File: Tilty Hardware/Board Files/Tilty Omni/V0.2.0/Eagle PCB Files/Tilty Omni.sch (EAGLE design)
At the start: 11 parts, among them U1 TEENSY_3.0_ALLPINS

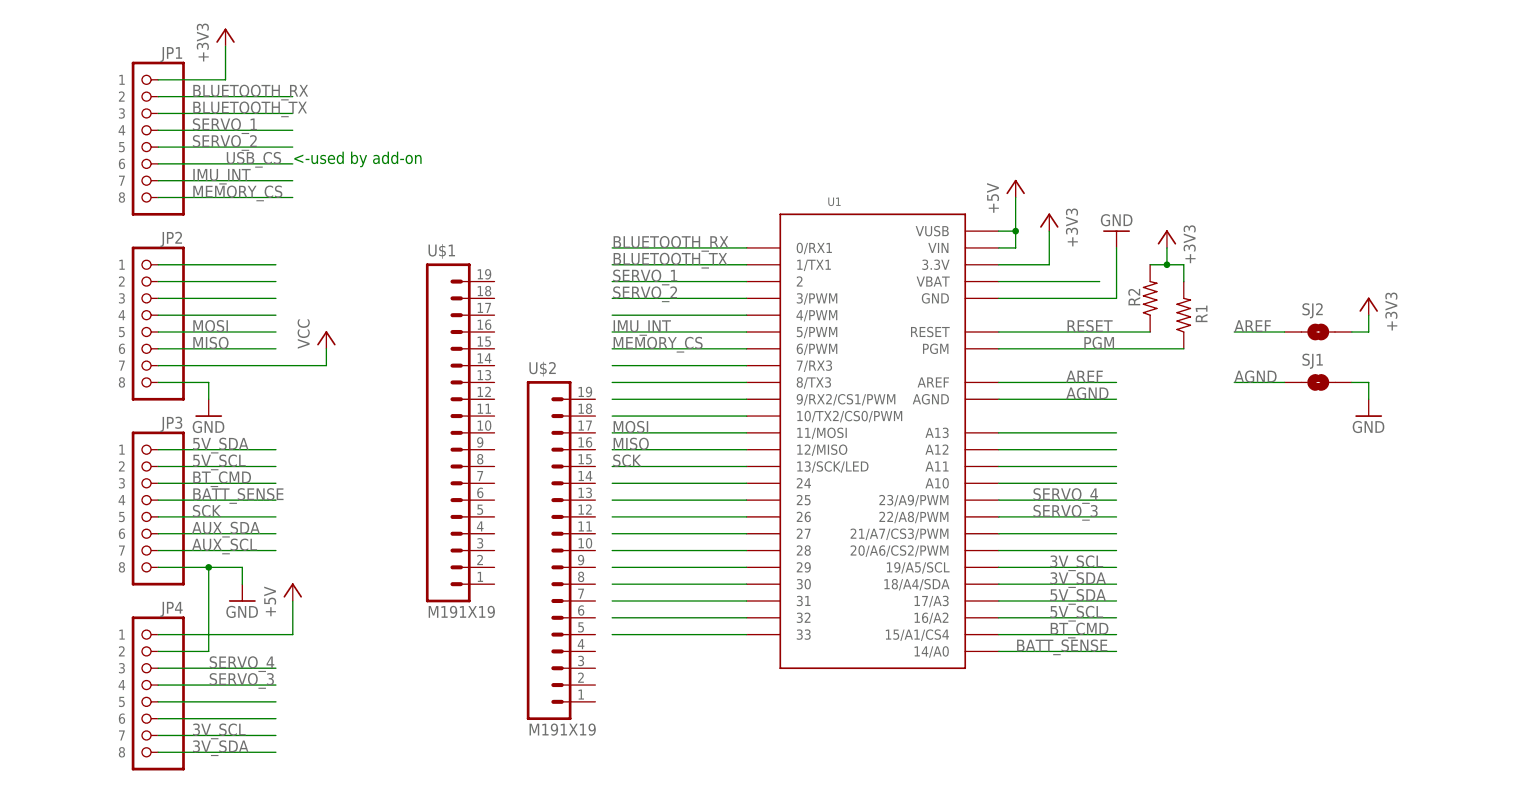
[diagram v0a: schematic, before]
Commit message: Updated Tilty Omni pinout and removed Eagle backup files,as that's what GitHub is for
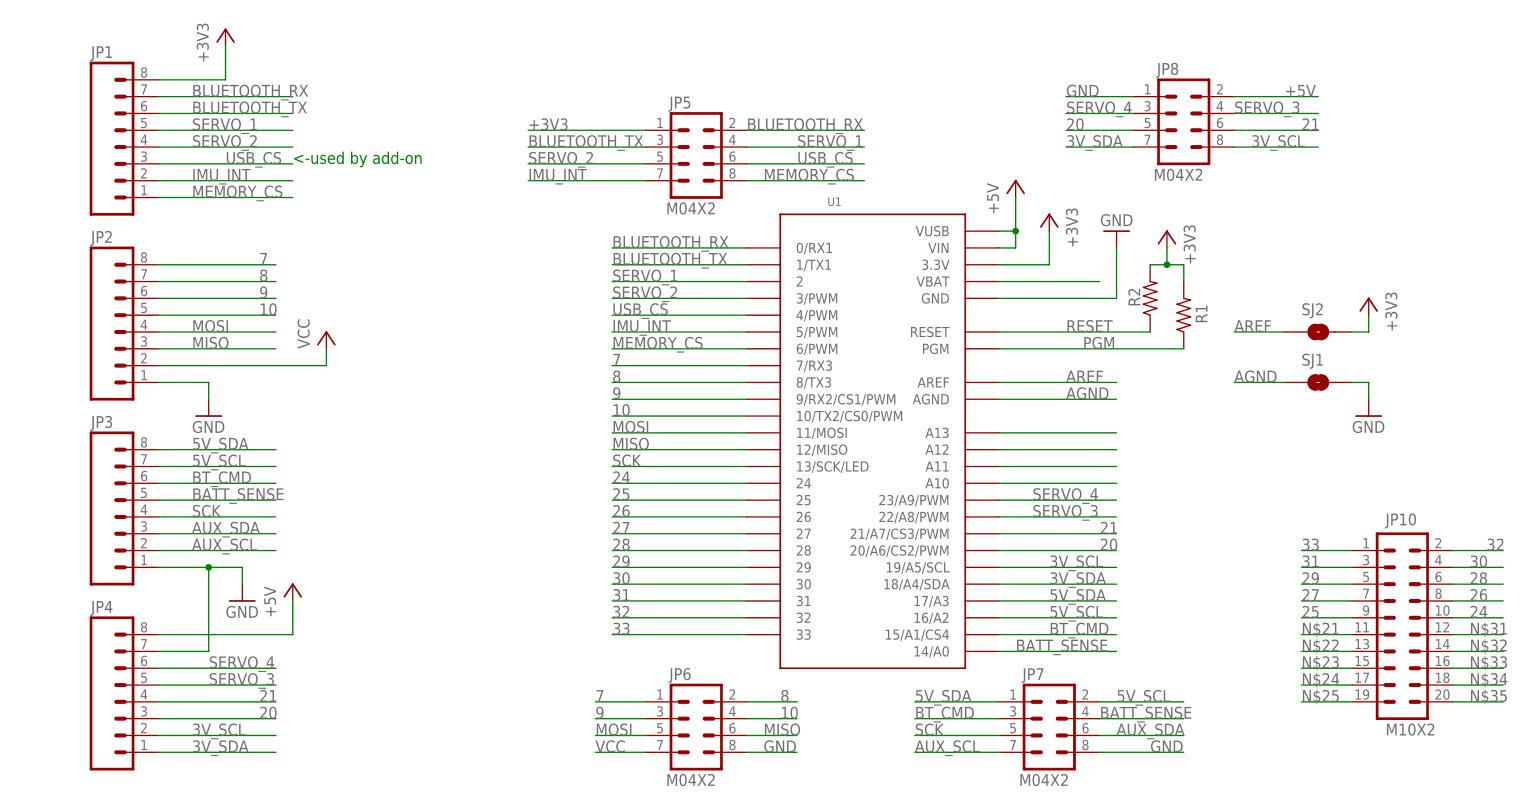
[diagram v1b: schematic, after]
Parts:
- removed U$1, U$2: M191X19, SparkFun-Connectors:M191X19
- added JP10: M10X2, SparkFun-Connectors:M10X2
- added JP5, JP6, JP7, JP8: M04X2, SparkFun-Connectors:M04X2
- JP1, JP2, JP3, JP4: value 8-PIN_HEADER -> (none); device My Parts:8-PIN_HEADER -> SparkFun-Connectors:M081X08
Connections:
- net N$14 renamed A13
- removed net N$1: U1.24
- removed net N$10: U1.33
- removed net N$2: U1.25
- removed net N$3: U1.26
- removed net N$4: U1.27
- removed net N$5: U1.28
- removed net N$6: U1.29
- removed net N$7: U1.30
- removed net N$8: U1.31
- removed net N$9: U1.32
- new net 24: JP10.10, U1.24
- new net 25: JP10.9, U1.25
- new net 26: JP10.8, U1.26
- new net 27: JP10.7, U1.27
- new net 28: JP10.6, U1.28
- new net 29: JP10.5, U1.29
- new net 30: JP10.4, U1.30
- new net 31: JP10.3, U1.31
- new net 32: JP10.2, U1.32
- new net 33: JP10.1, U1.33
- new net N$21: JP10.11
- new net N$22: JP10.13
- new net N$23: JP10.15
- new net N$24: JP10.17
- new net N$25: JP10.19
- new net N$31: JP10.12
- new net N$32: JP10.14
- new net N$33: JP10.16
- new net N$34: JP10.18
- new net N$35: JP10.20
- net +3V3: now also JP1.8, JP5.1; no longer JP1.1
- net +5V: now also JP4.8, JP8.2; no longer JP4.1
- net 10: now also JP2.5, JP6.4; no longer JP2.4
- net 20: now also JP4.3, JP8.5; no longer JP4.6
- net 21: now also JP4.4, JP8.6; no longer JP4.5
- net 3V_SCL: now also JP4.2, JP8.8; no longer JP4.7
- net 3V_SDA: now also JP4.1, JP8.7; no longer JP4.8
- net 5V_SCL: now also JP3.7, JP7.2; no longer JP3.2
- net 5V_SDA: now also JP3.8, JP7.1; no longer JP3.1
- net 7: now also JP2.8, JP6.1; no longer JP2.1
- net 8: now also JP2.7, JP6.2; no longer JP2.2
- net 9: now also JP2.6, JP6.3; no longer JP2.3
- net AUX_SCL: now also JP3.2, JP7.7; no longer JP3.7
- net AUX_SDA: now also JP3.3, JP7.6; no longer JP3.6
- net BATT_SENSE: now also JP3.5, JP7.4; no longer JP3.4
- net BLUETOOTH_RX: now also JP1.7, JP5.2; no longer JP1.2
- net BLUETOOTH_TX: now also JP1.6, JP5.3; no longer JP1.3
- net BT_CMD: now also JP3.6, JP7.3; no longer JP3.3
- net GND: now also JP2.1, JP3.1, JP4.7, JP6.8, JP7.8, JP8.1; no longer JP2.8, JP3.8, JP4.2
- net IMU_INT: now also JP1.2, JP5.7; no longer JP1.7
- net MEMORY_CS: now also JP1.1, JP5.8; no longer JP1.8
- net MISO: now also JP2.3, JP6.6; no longer JP2.6
- net MOSI: now also JP2.4, JP6.5; no longer JP2.5
- net SCK: now also JP3.4, JP7.5; no longer JP3.5
- net SERVO_1: now also JP1.5, JP5.4; no longer JP1.4
- net SERVO_2: now also JP1.4, JP5.5; no longer JP1.5
- net SERVO_3: now also JP4.5, JP8.4; no longer JP4.4
- net SERVO_4: now also JP4.6, JP8.3; no longer JP4.3
- net USB_CS: now also JP1.3, JP5.6; no longer JP1.6
- net VCC: now also JP2.2, JP6.7; no longer JP2.7
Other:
- moved on the sheet: JP1, JP2, JP3, JP4

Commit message: Tilty Omni work
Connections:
- net N$21 renamed A12
- net N$22 renamed A10
- net N$32 renamed A11
- removed net N$23: JP10.15
- removed net N$24: JP10.17
- removed net N$25: JP10.19
- removed net N$31: JP10.12
- removed net N$33: JP10.16
- removed net N$34: JP10.18
- removed net N$35: JP10.20
- net +3V3: now also JP10.19
- net A13: now also JP10.12
- net AGND: now also JP10.16
- net AREF: now also JP10.15
- net GND: now also JP10.20
- net PGM: now also JP10.17
- net RESET: now also JP10.18
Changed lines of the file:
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@@
 <label x="142.24" y="101.6" size="1.778" layer="95"/>
+</segment>
+<segment>
+<pinref part="JP10" gate="G$1" pin="20"/>
+<wire x1="200.66" y1="10.16" x2="208.28" y2="10.16" width="0.1524" layer="91"/>
+<label x="203.2" y="10.16" size="1.778" layer="95"/>
 </segment>
 </net>
@@
 <label x="60.96" y="96.52" size="1.778" layer="95"/>
 </segment>
+<segment>
+<pinref part="JP10" gate="G$1" pin="19"/>
+<wire x1="185.42" y1="10.16" x2="177.8" y2="10.16" width="0.1524" layer="91"/>
+<label x="177.8" y="10.16" size="1.778" layer="95"/>
+</segment>
 </net>
 <net name="+5V" class="0">
@@
 <pinref part="R2" gate="G$1" pin="1"/>
 </segment>
+<segment>
+<pinref part="JP10" gate="G$1" pin="18"/>
+<wire x1="200.66" y1="12.7" x2="208.28" y2="12.7" width="0.1524" layer="91"/>
+<label x="203.2" y="12.7" size="1.778" layer="95"/>
+</segment>
 </net>
 <net name="PGM" class="0">
@@
 <pinref part="R1" gate="G$1" pin="1"/>
 </segment>
+<segment>
+<pinref part="JP10" gate="G$1" pin="17"/>
+<wire x1="185.42" y1="12.7" x2="177.8" y2="12.7" width="0.1524" layer="91"/>
+<label x="177.8" y="12.7" size="1.778" layer="95"/>
+</segment>
 </net>
 <net name="N$11" class="0">
@@
 <label x="167.64" y="58.42" size="1.778" layer="95"/>
 </segment>
+<segment>
+<pinref part="JP10" gate="G$1" pin="16"/>
+<wire x1="200.66" y1="15.24" x2="208.28" y2="15.24" width="0.1524" layer="91"/>
+<label x="203.2" y="15.24" size="1.778" layer="95"/>
+</segment>
 </net>
 <net name="AREF" class="0">
@@
 <label x="167.64" y="66.04" size="1.778" layer="95"/>
 </segment>
+<segment>
+<pinref part="JP10" gate="G$1" pin="15"/>
+<wire x1="185.42" y1="15.24" x2="177.8" y2="15.24" width="0.1524" layer="91"/>
+<label x="177.8" y="15.24" size="1.778" layer="95"/>
+</segment>
 </net>
 <net name="N$17" class="0">
@@
 </segment>
 </net>
-<net name="N$21" class="0">
+<net name="A12" class="0">
 <segment>
 <pinref part="JP10" gate="G$1" pin="11"/>
@@
 </segment>
 </net>
-<net name="N$22" class="0">
+<net name="A10" class="0">
 <segment>
 <pinref part="JP10" gate="G$1" pin="13"/>
@@
 </segment>
 </net>
-<net name="N$23" class="0">
-<segment>
-<pinref part="JP10" gate="G$1" pin="15"/>
-<wire x1="185.42" y1="15.24" x2="177.8" y2="15.24" width="0.1524" layer="91"/>
-<label x="177.8" y="15.24" size="1.778" layer="95"/>
-</segment>
-</net>
-<net name="N$24" class="0">
-<segment>
-<pinref part="JP10" gate="G$1" pin="17"/>
-<wire x1="185.42" y1="12.7" x2="177.8" y2="12.7" width="0.1524" layer="91"/>
-<label x="177.8" y="12.7" size="1.778" layer="95"/>
-</segment>
-</net>
-<net name="N$25" class="0">
-<segment>
-<pinref part="JP10" gate="G$1" pin="19"/>
-<wire x1="185.42" y1="10.16" x2="177.8" y2="10.16" width="0.1524" layer="91"/>
-<label x="177.8" y="10.16" size="1.778" layer="95"/>
-</segment>
-</net>
 <net name="A13" class="0">
 <segment>
 <pinref part="U1" gate="G$1" pin="A13"/>
 <wire x1="132.08" y1="50.8" x2="149.86" y2="50.8" width="0.1524" layer="91"/>
+</segment>
+<segment>
+<pinref part="JP10" gate="G$1" pin="12"/>
+<wire x1="200.66" y1="20.32" x2="208.28" y2="20.32" width="0.1524" layer="91"/>
+<label x="203.2" y="20.32" size="1.778" layer="95"/>
 </segment>
 </net>
@@
 </segment>
 </net>
-<net name="N$31" class="0">
-<segment>
-<pinref part="JP10" gate="G$1" pin="12"/>
-<wire x1="200.66" y1="20.32" x2="208.28" y2="20.32" width="0.1524" layer="91"/>
-<label x="203.2" y="20.32" size="1.778" layer="95"/>
-</segment>
-</net>
-<net name="N$32" class="0">
+<net name="A11" class="0">
 <segment>
 <pinref part="JP10" gate="G$1" pin="14"/>
@@
 </segment>
 </net>
-<net name="N$33" class="0">
-<segment>
-<pinref part="JP10" gate="G$1" pin="16"/>
-<wire x1="200.66" y1="15.24" x2="208.28" y2="15.24" width="0.1524" layer="91"/>
-<label x="203.2" y="15.24" size="1.778" layer="95"/>
-</segment>
-</net>
-<net name="N$34" class="0">
-<segment>
-<pinref part="JP10" gate="G$1" pin="18"/>
-<wire x1="200.66" y1="12.7" x2="208.28" y2="12.7" width="0.1524" layer="91"/>
-<label x="203.2" y="12.7" size="1.778" layer="95"/>
-</segment>
-</net>
-<net name="N$35" class="0">
-<segment>
-<pinref part="JP10" gate="G$1" pin="20"/>
-<wire x1="200.66" y1="10.16" x2="208.28" y2="10.16" width="0.1524" layer="91"/>
-<label x="203.2" y="10.16" size="1.778" layer="95"/>
-</segment>
-</net>

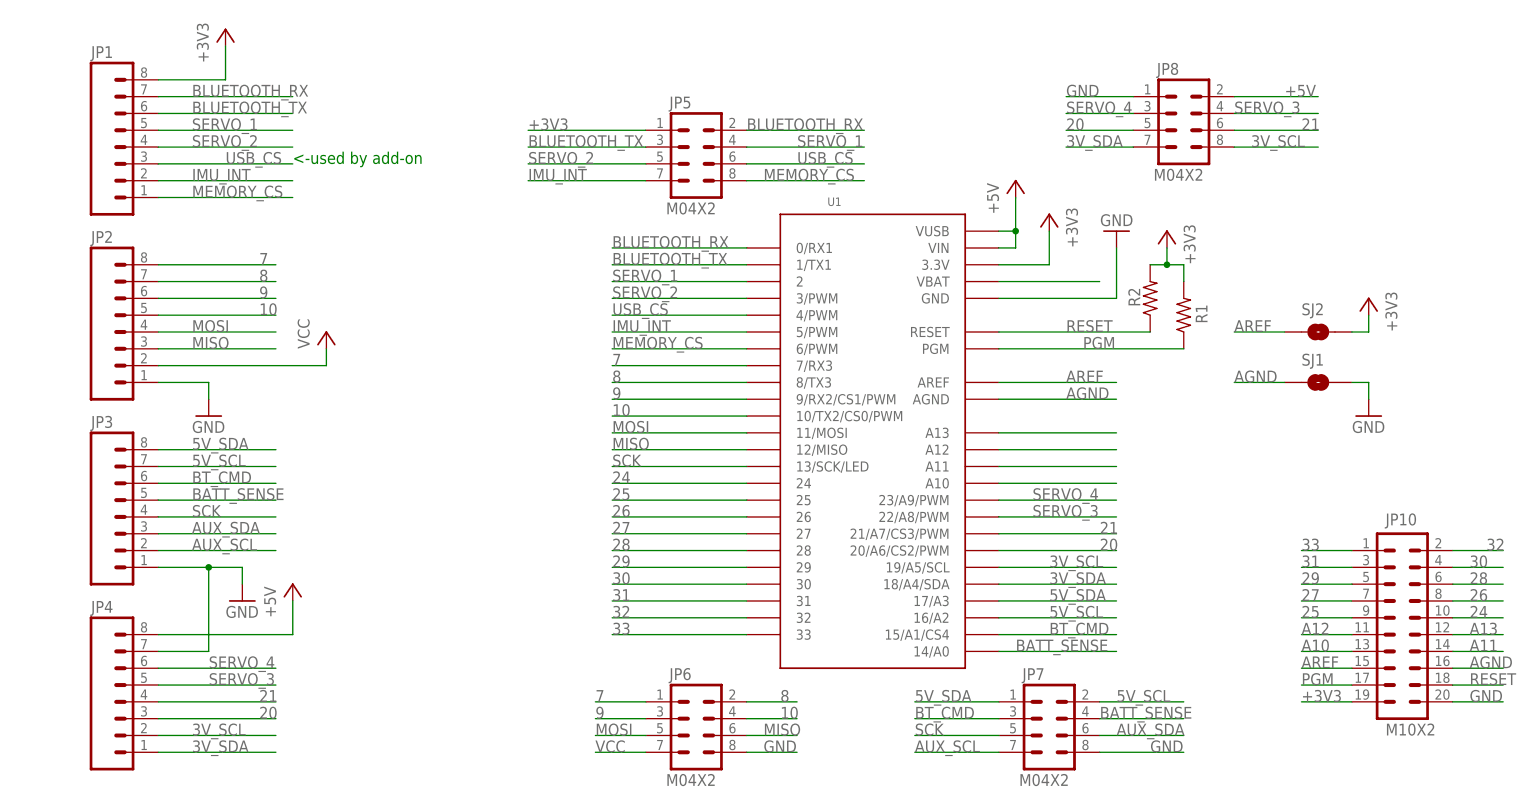
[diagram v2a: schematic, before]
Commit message: Deleted redundant Tilty Omni backups
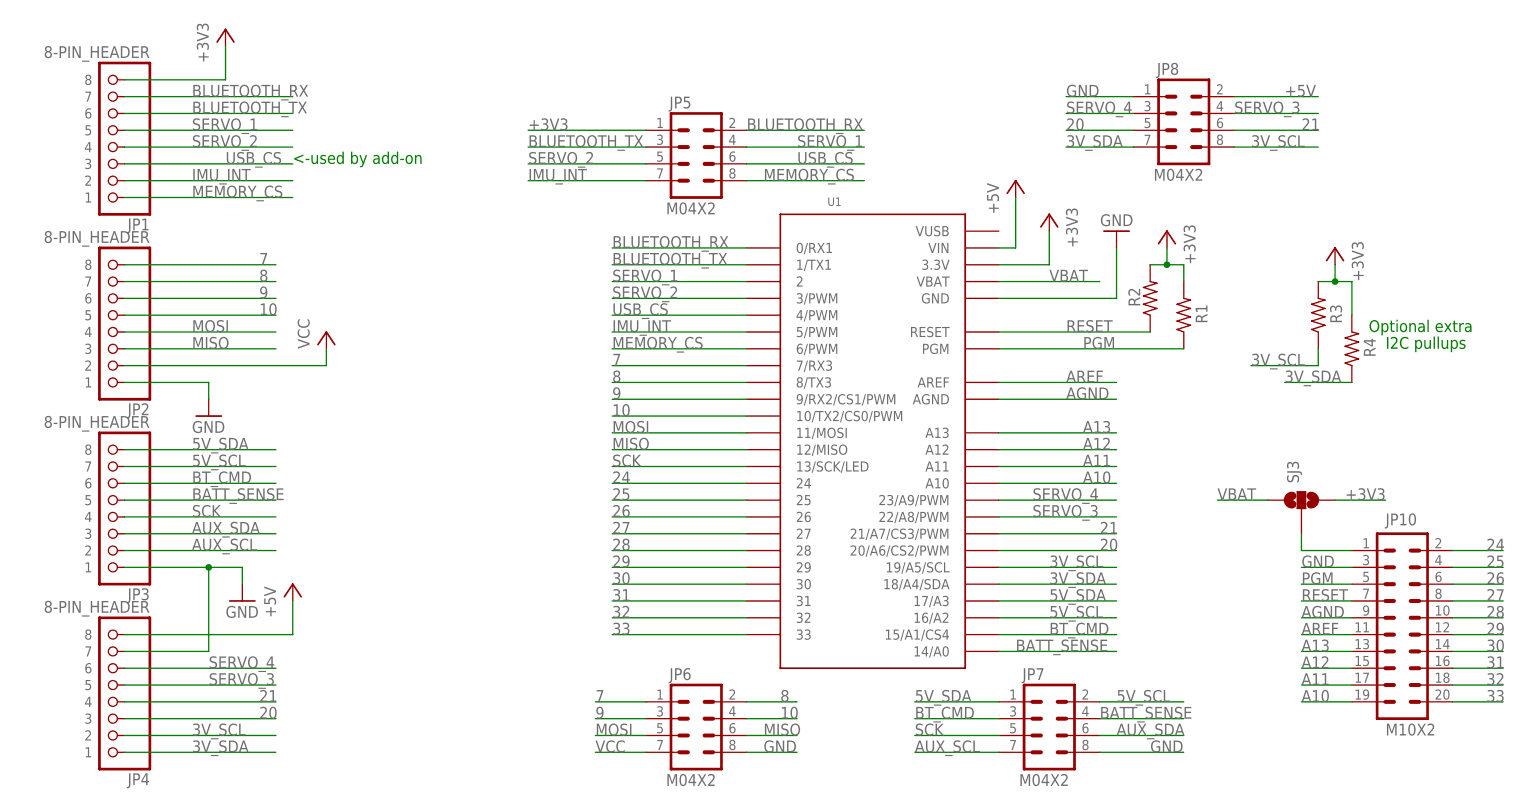
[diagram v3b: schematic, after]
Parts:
- removed SJ1, SJ2: SOLDERJUMPERTRACE, SparkFun-Passives:SOLDERJUMPERTRACE
- added R3, R4: 10k, resistor:R-US_R0603
- added SJ3: (no value), SparkFun-Passives:SOLDERJUMPER_2WAYPASTE2&3
- JP1, JP2, JP3, JP4: value (none) -> 8-PIN_HEADER; device SparkFun-Connectors:M081X08 -> My Parts:8-PIN_HEADER
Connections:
- removed net N$11: U1.A10
- removed net N$12: U1.A11
- removed net N$13: U1.A12
- removed net N$17: U1.VBAT
- new net N$2: JP10.1, SJ3.2
- new net VBAT: SJ3.1, U1.VBAT
- net +3V3: now also R3.2, R4.2, SJ3.3; no longer JP10.19, SJ2.2
- net +5V: no longer U1.VUSB
- net 24: now also JP10.2; no longer JP10.10
- net 25: now also JP10.4; no longer JP10.9
- net 26: now also JP10.6; no longer JP10.8
- net 27: now also JP10.8; no longer JP10.7
- net 28: now also JP10.10; no longer JP10.6
- net 29: now also JP10.12; no longer JP10.5
- net 30: now also JP10.14; no longer JP10.4
- net 31: now also JP10.16; no longer JP10.3
- net 32: now also JP10.18; no longer JP10.2
- net 33: now also JP10.20; no longer JP10.1
- net 3V_SCL: now also R3.1
- net 3V_SDA: now also R4.1
- net A10: now also JP10.19, U1.A10; no longer JP10.13
- net A11: now also JP10.17, U1.A11; no longer JP10.14
- net A12: now also JP10.15, U1.A12; no longer JP10.11
- net A13: now also JP10.13; no longer JP10.12
- net AGND: now also JP10.9; no longer JP10.16, SJ1.1
- net AREF: now also JP10.11; no longer JP10.15, SJ2.1
- net GND: now also JP10.3; no longer JP10.20, SJ1.2
- net PGM: now also JP10.5; no longer JP10.17
- net RESET: now also JP10.7; no longer JP10.18
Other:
- note added: "I2C pullups"
- note added: "Optional extra"
- moved on the sheet: JP1, JP2, JP3, JP4
